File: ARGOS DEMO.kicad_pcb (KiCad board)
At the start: 4 copper layers, 50 x 80 mm, 91 parts, among them J1 B2B-XH-A, J2 60312002114503, J3 B4B-XH-A, J4 JTAG 10-PINS, J5 B4B-XH-A, J6 B6B-XH-A, J7 B3B-XH-A, J8 USB4085-GF-A, Q1 BSN20, Q2 BSN20, SW1 PTS647, U1 Argos SMD module, U2 LTC4365DDB, U3 TPS63900, U4 TPS63900, U5 82400102, U6 FT231XQ

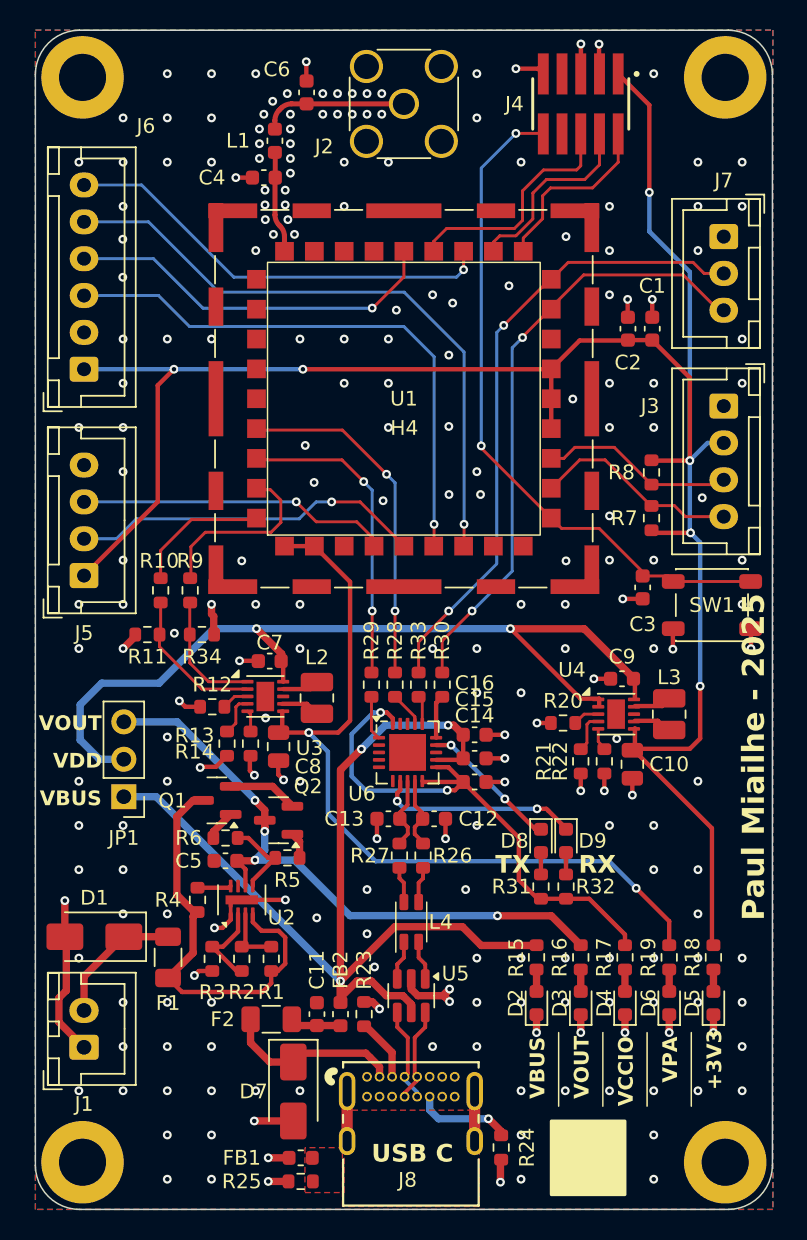
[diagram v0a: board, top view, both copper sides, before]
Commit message: Correction USART vers le LPUART
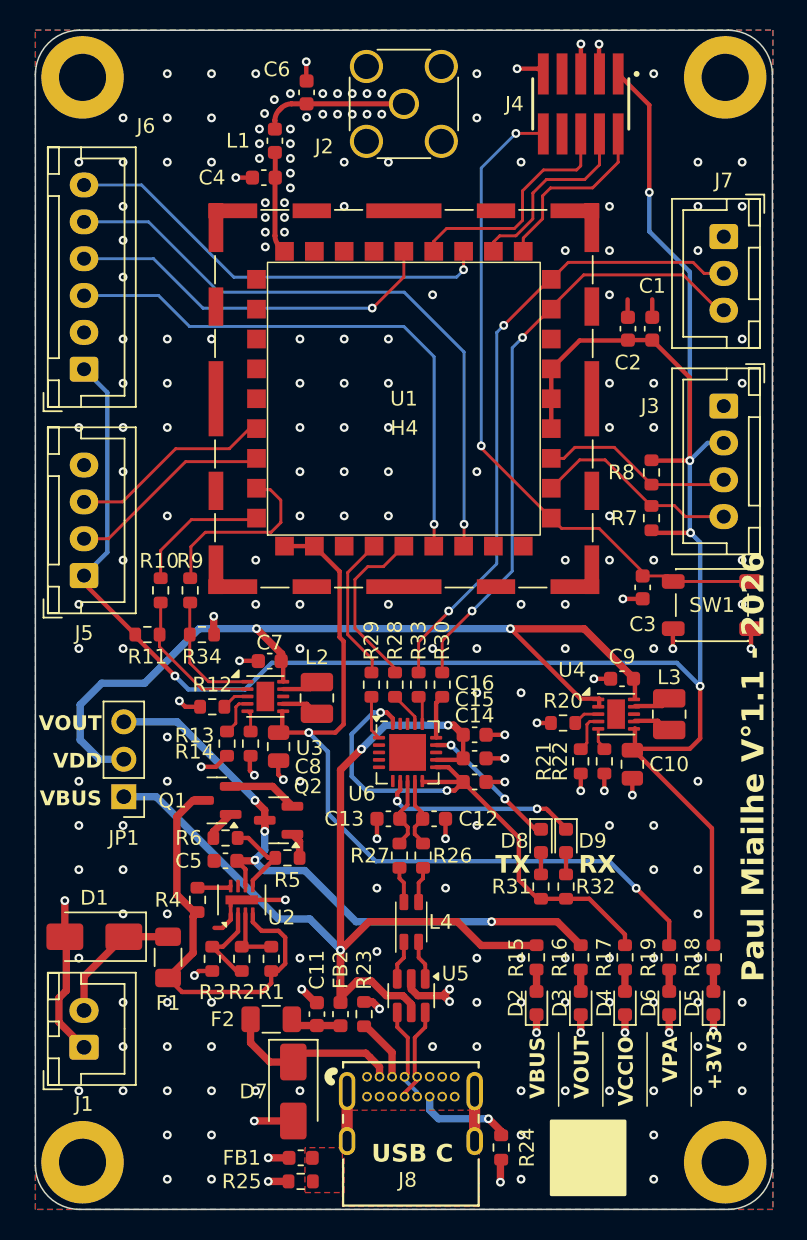
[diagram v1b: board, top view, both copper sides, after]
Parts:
- moved G*** 0.51 mm to (126.0, 85.0)
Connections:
- J5 pad 2: /LPUART_RX -> /UART_TX
- J5 pad 3: /LPUART_TX -> /UART_RX
- R11 pad 2: GND -> +3V3
- R28 pad 2: /UART_RX -> /LPUART_RX
- R29 pad 2: /UART_TX -> /LPUART_TX
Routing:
- net +3V3: track 146.7 -> 160.8 mm, vias 6 -> 5
- net /LPUART_RX: track 24.0 -> 11.7 mm, vias 1 -> 0
- net /LPUART_TX: track 21.2 -> 10.0 mm, vias 1 -> 0
- net /UART_RX: track 23.7 -> 13.8 mm, vias 2 -> 0
- net /UART_TX: track 21.1 -> 14.0 mm, vias 2 -> 0
- net GND: track 74.3 -> 73.6 mm, vias 226 -> 219
- net VBUS: track 74.2 -> 74.8 mm
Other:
- board text added: "Paul Miailhe V°1.1 - 2026"
- board text removed: "Paul Miailhe - 2025"

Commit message: update doc
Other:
- board text added: "Paul Miailhe V°1.2 - 2026"
- board text removed: "Paul Miailhe V°1.1 - 2026"
